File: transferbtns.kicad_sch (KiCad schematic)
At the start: 11 parts, among them U2 74LS165

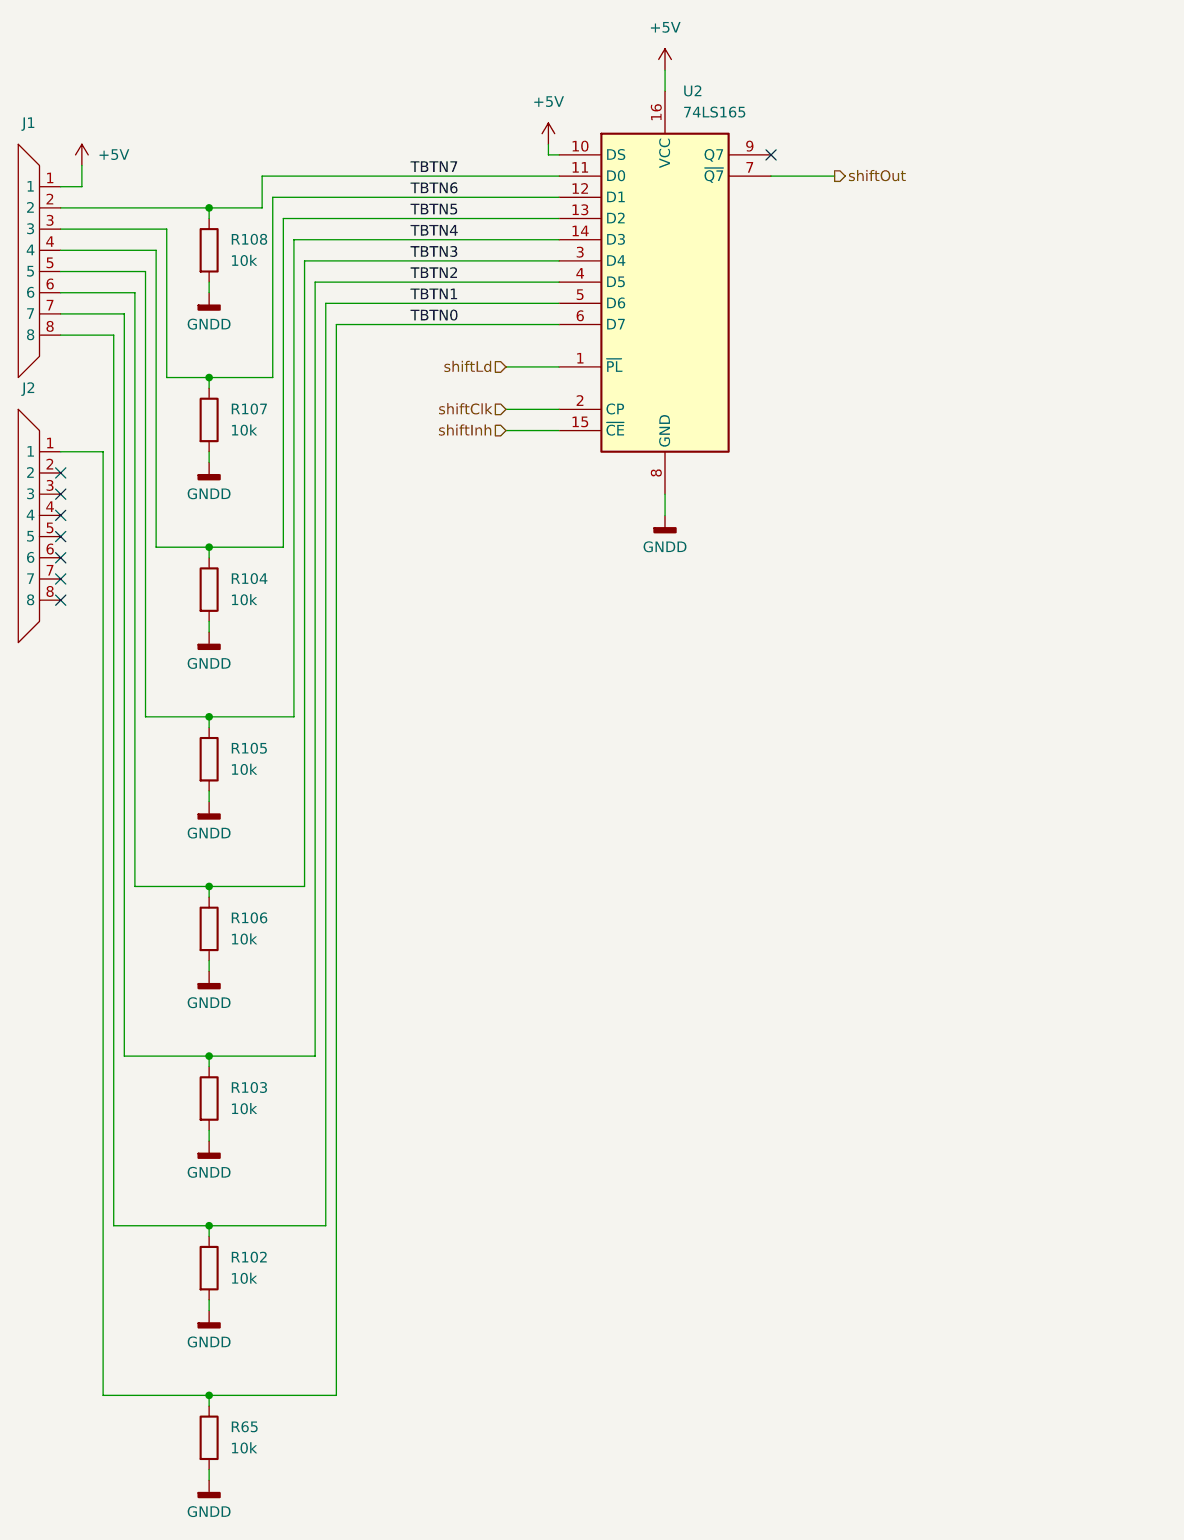
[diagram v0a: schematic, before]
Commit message: start connecting subsheets to main schematic
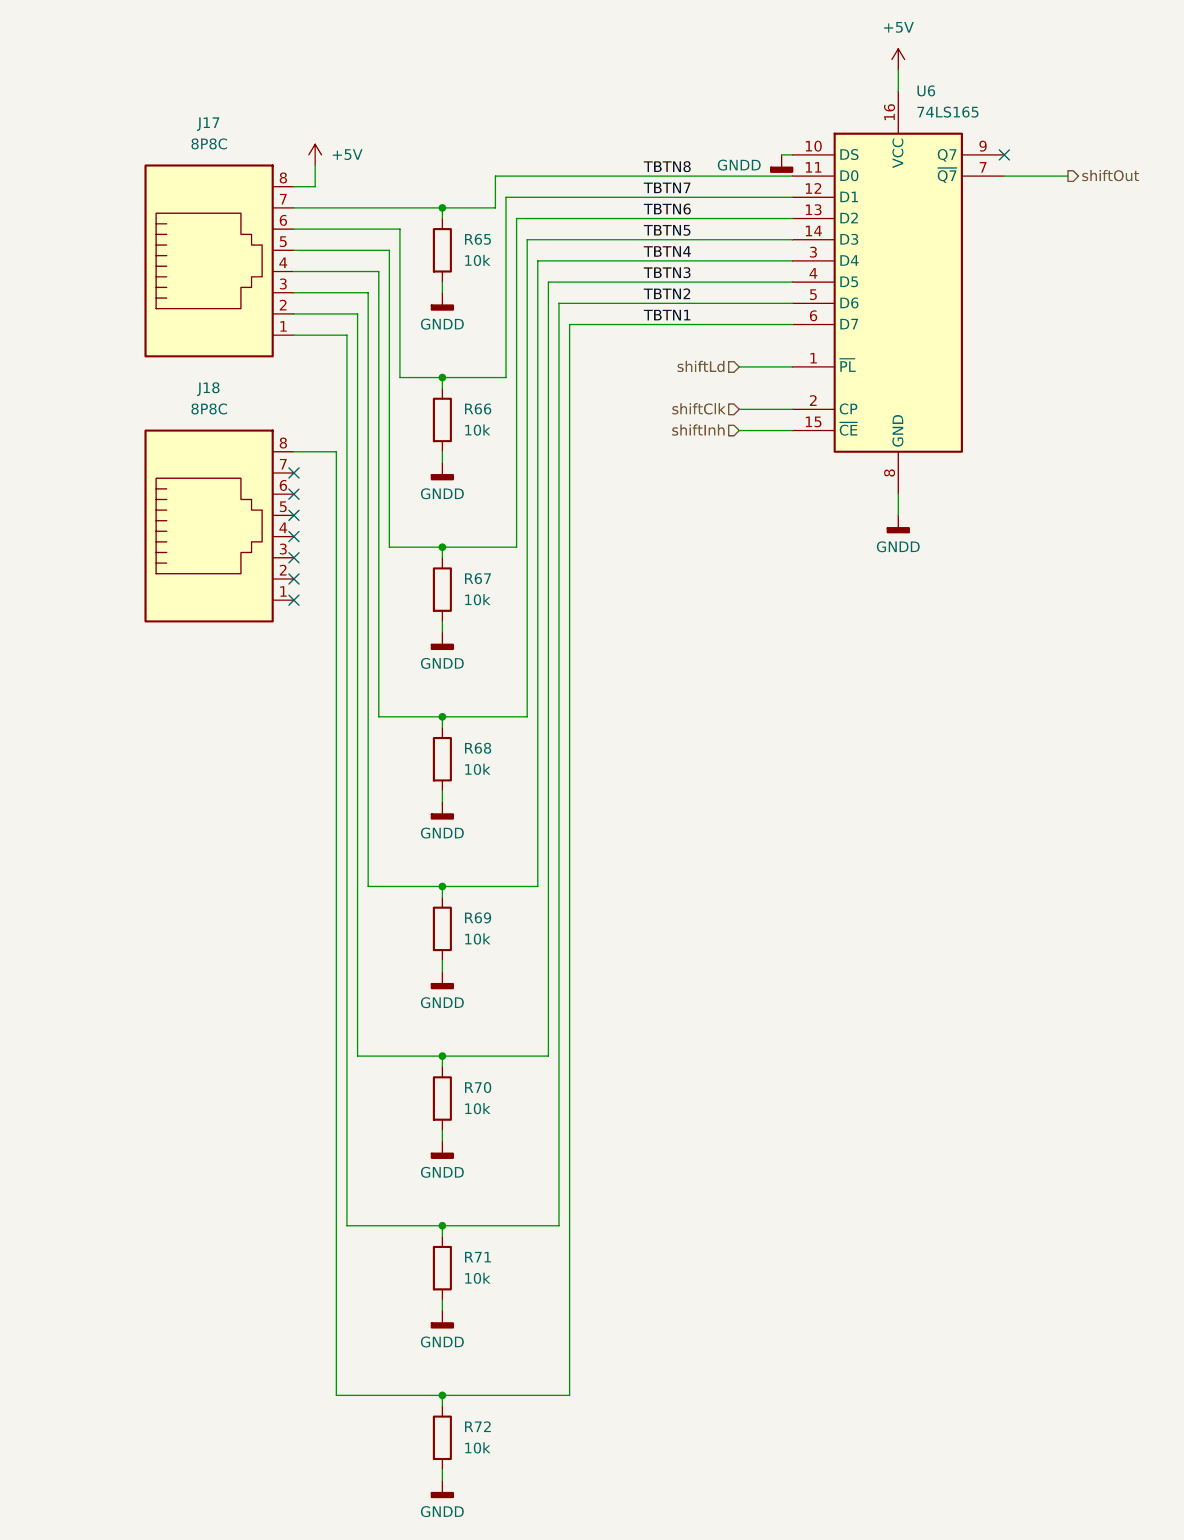
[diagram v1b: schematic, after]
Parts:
- removed J1, J2: (no value), symbol Phones:8C_Connector
- added J17, J18: 8P8C, symbol Connector:8P8C
- renumbered R108 to R65, R107 to R66, R104 to R67, R105 to R68, R106 to R69, R103 to R70, R102 to R71, R65 to R72, U2 to U6
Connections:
- net TBTN0 is gone; now on net TBTN1: R72.1, U6.6 (D7)
- net +5V: now also J17.8; no longer U6.10 (DS)
- net GNDD: now also U6.10 (DS)
- net TBTN1: now also J18.8; no longer R71.1, U6.5 (D6)
- net TBTN2: now also R71.1, U6.5 (D6), J17.1; no longer R70.1, U6.4 (D5)
- net TBTN3: now also R70.1, U6.4 (D5), J17.2; no longer R69.1, U6.3 (D4)
- net TBTN4: now also R69.1, U6.3 (D4), J17.3; no longer R68.1, U6.14 (D3)
- net TBTN5: now also R68.1, U6.14 (D3), J17.4; no longer R67.1, U6.13 (D2)
- net TBTN6: now also R67.1, U6.13 (D2), J17.5; no longer R66.1, U6.12 (D1)
- net TBTN7: now also R66.1, U6.12 (D1), J17.6; no longer R65.1, U6.11 (D0)
- new net TBTN8: J17.7, R65.1, U6.11 (D0)
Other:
- moved on the sheet: R65, R66, R67, R68, R69, R70, R71, R72, U6

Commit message: finish schematic capture
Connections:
- net +5V: now also J18.8; no longer J17.8
- net TBTN1: now also J17.1; no longer J18.8
- net TBTN2: now also J17.2; no longer J17.1
- net TBTN3: now also J17.3; no longer J17.2
- net TBTN4: now also J17.4; no longer J17.3
- net TBTN5: now also J17.5; no longer J17.4
- net TBTN6: now also J17.6; no longer J17.5
- net TBTN7: now also J17.7; no longer J17.6
- net TBTN8: now also J17.8; no longer J17.7
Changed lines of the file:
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@@
 	)
 	(junction
-		(at 85.09 38.1)
+		(at 85.09 35.56)
 		(diameter 0)
 		(color 0 0 0 0)
@@
 	(wire
 		(pts
-			(xy 73.66 160.02) (xy 73.66 53.34)
+			(xy 73.66 160.02) (xy 73.66 50.8)
 		)
 		(stroke
@@
 	(wire
 		(pts
-			(xy 77.47 99.06) (xy 77.47 45.72)
+			(xy 77.47 99.06) (xy 77.47 43.18)
 		)
 		(stroke
@@
 	(wire
 		(pts
+			(xy 85.09 35.56) (xy 85.09 39.37)
+		)
+		(stroke
+			(width 0)
+			(type default)
+		)
+	)
+	(wire
+		(pts
 			(xy 100.33 180.34) (xy 100.33 52.07)
 		)
@@
 	(wire
 		(pts
-			(xy 77.47 45.72) (xy 67.31 45.72)
+			(xy 77.47 43.18) (xy 67.31 43.18)
 		)
 		(stroke
@@
 	(wire
 		(pts
-			(xy 78.74 78.74) (xy 78.74 43.18)
-		)
-		(stroke
-			(width 0)
-			(type default)
-		)
-	)
-	(wire
-		(pts
-			(xy 91.44 38.1) (xy 85.09 38.1)
+			(xy 78.74 78.74) (xy 78.74 40.64)
+		)
+		(stroke
+			(width 0)
+			(type default)
+		)
+	)
+	(wire
+		(pts
+			(xy 91.44 35.56) (xy 85.09 35.56)
 		)
 		(stroke
@@
 	(wire
 		(pts
-			(xy 78.74 43.18) (xy 67.31 43.18)
+			(xy 67.31 67.31) (xy 68.58 67.31)
+		)
+		(stroke
+			(width 0)
+			(type default)
+		)
+	)
+	(wire
+		(pts
+			(xy 78.74 40.64) (xy 67.31 40.64)
 		)
 		(stroke
@@
 	(wire
 		(pts
-			(xy 74.93 50.8) (xy 67.31 50.8)
-		)
-		(stroke
-			(width 0)
-			(type default)
-		)
-	)
-	(wire
-		(pts
-			(xy 76.2 119.38) (xy 76.2 48.26)
+			(xy 74.93 48.26) (xy 67.31 48.26)
+		)
+		(stroke
+			(width 0)
+			(type default)
+		)
+	)
+	(wire
+		(pts
+			(xy 76.2 119.38) (xy 76.2 45.72)
 		)
 		(stroke
@@
 	(wire
 		(pts
-			(xy 73.66 53.34) (xy 67.31 53.34)
-		)
-		(stroke
-			(width 0)
-			(type default)
-		)
-	)
-	(wire
-		(pts
-			(xy 91.44 34.29) (xy 91.44 38.1)
+			(xy 73.66 50.8) (xy 67.31 50.8)
+		)
+		(stroke
+			(width 0)
+			(type default)
+		)
+	)
+	(wire
+		(pts
+			(xy 91.44 34.29) (xy 91.44 35.56)
 		)
 		(stroke
@@
 	(wire
 		(pts
-			(xy 67.31 35.56) (xy 69.85 35.56)
-		)
-		(stroke
-			(width 0)
-			(type default)
-		)
-	)
-	(wire
-		(pts
 			(xy 85.09 128.27) (xy 85.09 129.54)
 		)
@@
 	(wire
 		(pts
+			(xy 68.58 66.04) (xy 68.58 67.31)
+		)
+		(stroke
+			(width 0)
+			(type default)
+		)
+	)
+	(wire
+		(pts
 			(xy 85.09 160.02) (xy 99.06 160.02)
 		)
@@
 	(wire
 		(pts
-			(xy 69.85 33.02) (xy 69.85 35.56)
-		)
-		(stroke
-			(width 0)
-			(type default)
-		)
-	)
-	(wire
-		(pts
 			(xy 85.09 168.91) (xy 85.09 170.18)
 		)
@@
 	(wire
 		(pts
-			(xy 72.39 180.34) (xy 72.39 67.31)
+			(xy 72.39 180.34) (xy 72.39 53.34)
 		)
 		(stroke
@@
 	(wire
 		(pts
-			(xy 76.2 48.26) (xy 67.31 48.26)
+			(xy 76.2 45.72) (xy 67.31 45.72)
 		)
 		(stroke
@@
 	(wire
 		(pts
-			(xy 74.93 139.7) (xy 74.93 50.8)
-		)
-		(stroke
-			(width 0)
-			(type default)
-		)
-	)
-	(wire
-		(pts
-			(xy 85.09 38.1) (xy 85.09 39.37)
+			(xy 74.93 139.7) (xy 74.93 48.26)
 		)
 		(stroke
@@
 	(wire
 		(pts
-			(xy 80.01 40.64) (xy 67.31 40.64)
+			(xy 80.01 38.1) (xy 67.31 38.1)
 		)
 		(stroke
@@
 	(wire
 		(pts
-			(xy 72.39 67.31) (xy 67.31 67.31)
+			(xy 72.39 53.34) (xy 67.31 53.34)
 		)
 		(stroke
@@
 	(wire
 		(pts
-			(xy 80.01 58.42) (xy 80.01 40.64)
-		)
-		(stroke
-			(width 0)
-			(type default)
-		)
-	)
-	(wire
-		(pts
-			(xy 67.31 38.1) (xy 85.09 38.1)
+			(xy 80.01 58.42) (xy 80.01 38.1)
+		)
+		(stroke
+			(width 0)
+			(type default)
+		)
+	)
+	(wire
+		(pts
+			(xy 67.31 35.56) (xy 85.09 35.56)
 		)
 		(stroke
@@
 	)
 	(symbol
-		(lib_id "power:+5V")
-		(at 69.85 33.02 0)
-		(unit 1)
-		(body_style 1)
-		(exclude_from_sim no)
-		(in_bom yes)
-		(on_board yes)
-		(in_pos_files yes)
-		(dnp no)
-		(property "Reference" "#PWR?"
-			(at 69.85 36.83 0)
-			(hide yes)
-			(show_name no)
-			(do_not_autoplace no)
-			(effects
-				(font
-					(size 1.27 1.27)
-				)
-			)
-		)
-		(property "Value" "+5V"
-			(at 73.66 31.75 0)
-			(show_name no)
-			(do_not_autoplace no)
-			(effects
-				(font
-					(size 1.27 1.27)
-				)
-			)
-		)
-		(property "Footprint" ""
-			(at 69.85 33.02 0)
-			(hide yes)
-			(show_name no)
-			(do_not_autoplace no)
-			(effects
-				(font
-					(size 1.27 1.27)
-				)
-			)
-		)
-		(property "Datasheet" ""
-			(at 69.85 33.02 0)
-			(hide yes)
-			(show_name no)
-			(do_not_autoplace no)
-			(effects
-				(font
-					(size 1.27 1.27)
-				)
-			)
-		)
-		(property "Description" "Power symbol creates a global label with name \"+5V\""
-			(at 69.85 33.02 0)
-			(hide yes)
-			(show_name no)
-			(do_not_autoplace no)
-			(effects
-				(font
-					(size 1.27 1.27)
-				)
-			)
-		)
-		(pin "1"
-		)
-		(instances
-			(project "pbx-sniffer-v2"
-				(path "/eb421281-26a1-483f-b39a-0425ec8eb8df/e4c2ebee-8cf8-408f-ab71-48d7afe9e7e1"
-					(reference "#PWR?")
-					(unit 1)
-				)
-			)
-		)
-	)
-	(symbol
 		(lib_id "power:GNDD")
 		(at 85.09 109.22 0)
@@
 					(unit 1)
 				)
+			)
+		)
+	)
+	(symbol
+		(lib_id "power:+5V")
+		(at 68.58 66.04 0)
+		(unit 1)
+		(body_style 1)
+		(exclude_from_sim no)
+		(in_bom yes)
+		(on_board yes)
+		(in_pos_files yes)
+		(dnp no)
+		(fields_autoplaced yes)
+		(property "Reference" "#PWR010"
+			(at 68.58 69.85 0)
+			(hide yes)
+			(show_name no)
+			(do_not_autoplace no)
+			(effects
+				(font
+					(size 1.27 1.27)
+				)
+			)
+		)
+		(property "Value" "+5V"
+			(at 68.58 60.96 0)
+			(show_name no)
+			(do_not_autoplace no)
+			(effects
+				(font
+					(size 1.27 1.27)
+				)
+			)
+		)
+		(property "Footprint" ""
+			(at 68.58 66.04 0)
+			(hide yes)
+			(show_name no)
+			(do_not_autoplace no)
+			(effects
+				(font
+					(size 1.27 1.27)
+				)
+			)
+		)
+		(property "Datasheet" ""
+			(at 68.58 66.04 0)
+			(hide yes)
+			(show_name no)
+			(do_not_autoplace no)
+			(effects
+				(font
+					(size 1.27 1.27)
+				)
+			)
+		)
+		(property "Description" "Power symbol creates a global label with name \"+5V\""
+			(at 68.58 66.04 0)
+			(hide yes)
+			(show_name no)
+			(do_not_autoplace no)
+			(effects
+				(font
+					(size 1.27 1.27)
+				)
+			)
+		)
+		(pin "1"
+		)
+		(instances
+			(project "pbx-sniffer-v2"
+				(path "/eb421281-26a1-483f-b39a-0425ec8eb8df/e4c2ebee-8cf8-408f-ab71-48d7afe9e7e1"
+					(reference "#PWR010")
+					(unit 1)
+				)

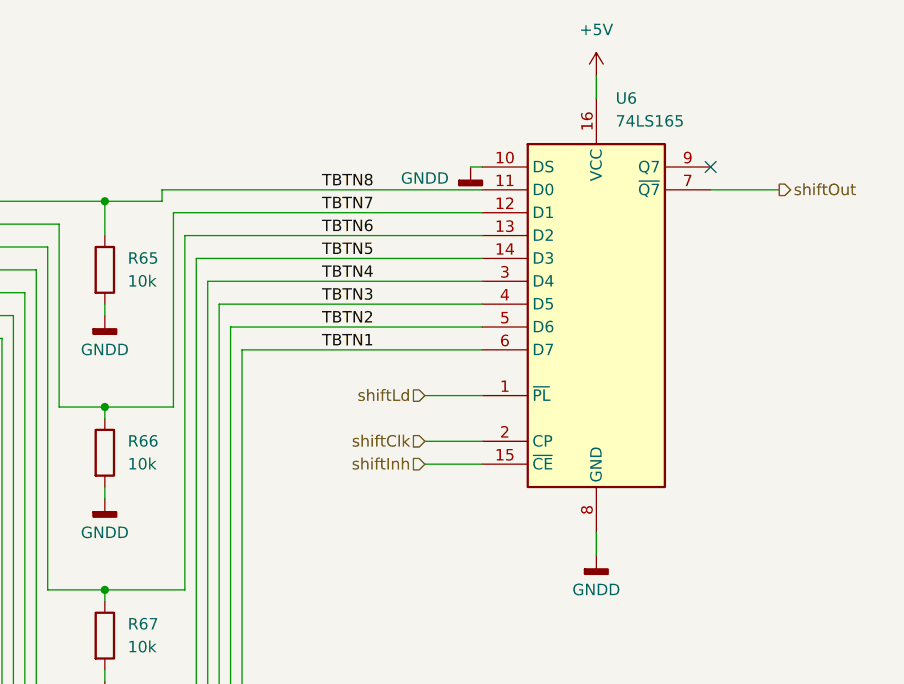
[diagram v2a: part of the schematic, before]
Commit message: add test points throughout the schematic
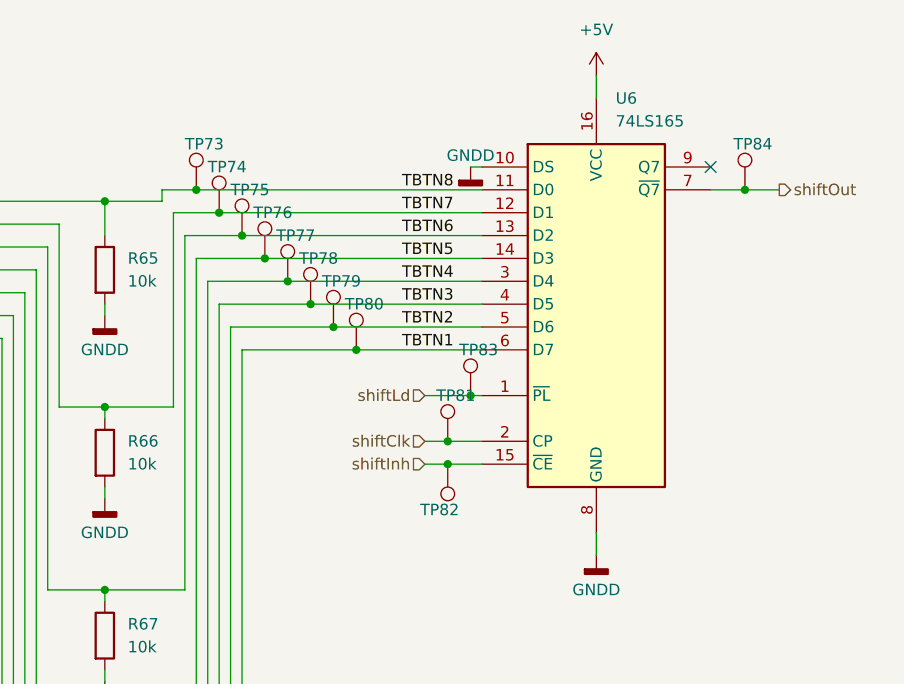
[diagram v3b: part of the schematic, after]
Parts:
- added TP73, TP74, TP75, TP76, TP77, TP78, TP79, TP80, TP81, TP82, TP83, TP84: TestPoint, Testpoints:M5_3in1_TestPoint, symbol Connector:TestPoint
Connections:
- net TBTN1: now also TP80.1
- net TBTN2: now also TP79.1
- net TBTN3: now also TP78.1
- net TBTN4: now also TP77.1
- net TBTN5: now also TP76.1
- net TBTN6: now also TP75.1
- net TBTN7: now also TP74.1
- net TBTN8: now also TP73.1
- net shiftClk: now also TP81.1
- net shiftInh: now also TP82.1
- net shiftLd: now also TP83.1
- net shiftOut: now also TP84.1
